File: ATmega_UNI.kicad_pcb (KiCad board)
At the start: 2 copper layers, 53.3 x 68.6 mm, 44 parts, among them J1 PDIP_1_to_14, J11 PDIP_1_to_14, J13 3.3V, J2 PDIP_15_to_28, J22 PDIP_15_to_28, J5 PWR_Jack, J611 I2C, J612 I2C, J62 4uni, J63 4uni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

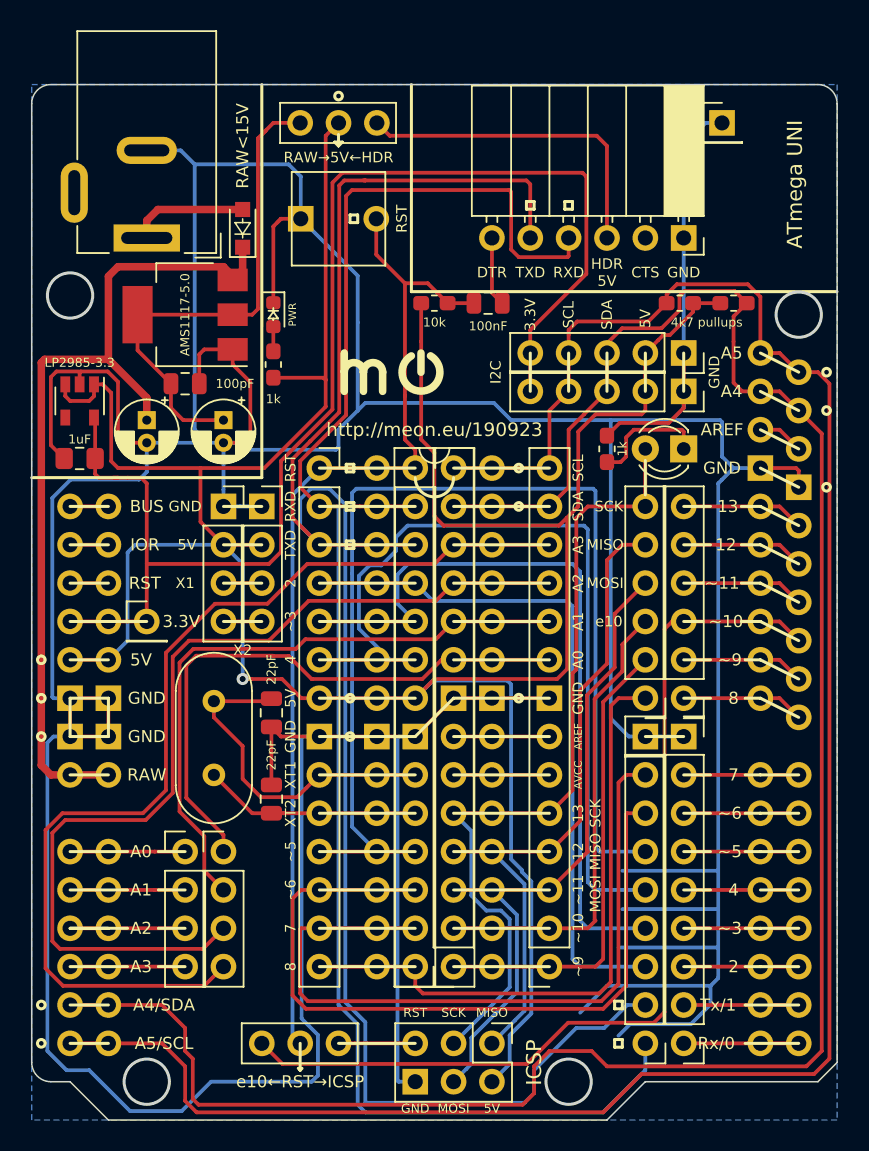
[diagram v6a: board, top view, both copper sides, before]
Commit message: move i2c to have more space for zif socket, wider 5V from raw tracks
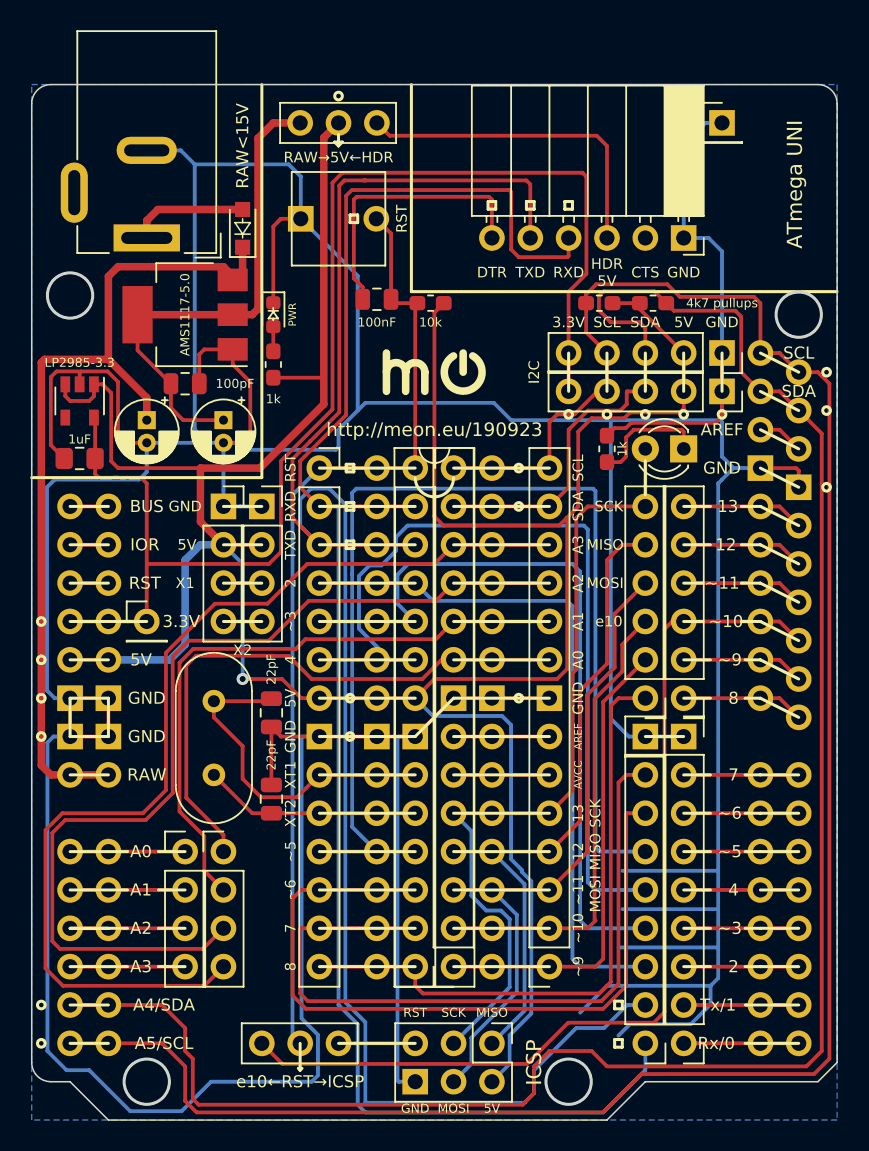
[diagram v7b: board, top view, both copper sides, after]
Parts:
- moved C2 7.37 mm to (88.9, 59.9), turned to 180 degrees
- moved R1 5.33 mm to (107.2, 60.2)
- moved R3 5.33 mm to (103.6, 60.2)
- moved REF** 2.79 mm to (92.7, 64.8)
- moved J611 2.54 mm to (111.8, 66.0)
- moved J612 2.54 mm to (111.8, 63.5)
- moved R2 0.25 mm to (92.5, 60.2), turned to 180 degrees
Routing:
- net DTR: track 4.60 -> 18.7 mm
- net GND: track 414.4 -> 423.5 mm
- net SDA: track 142.4 -> 148.1 mm
- net ~RST: track 68.0 -> 64.0 mm
- net SCL: track 139.5 -> 141.8 mm
- net +5V: track 196.3 -> 194.9 mm
- net +3V3: track 90.0 -> 89.0 mm
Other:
- net class wide added: clearance 0.2, trace_width 0.5, via_dia 0.8, via_drill 0.4

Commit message: move reset jumper a little further from icsp
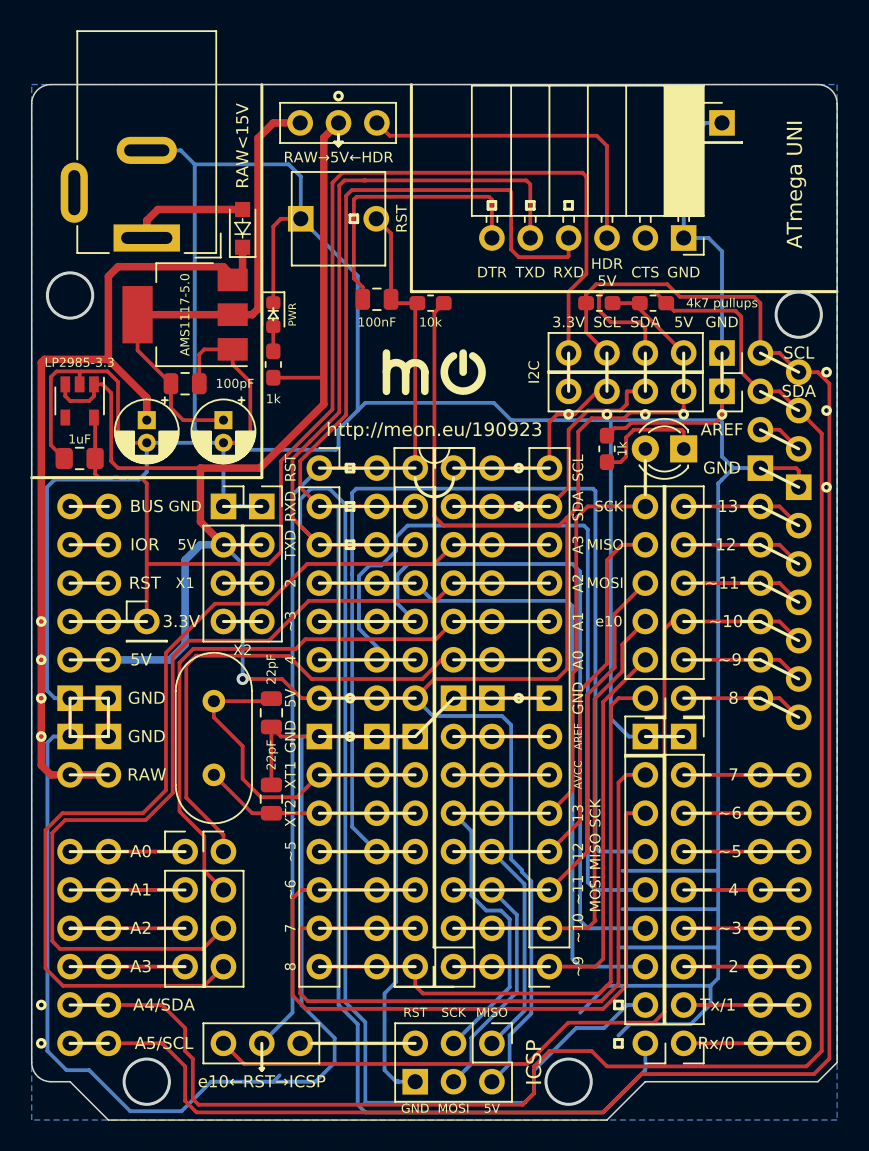
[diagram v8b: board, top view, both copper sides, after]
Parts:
- moved JP8 2.54 mm to (83.8, 109.2)
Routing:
- net ~iRST: track 5.08 -> 8.34 mm
- net GND: track 423.5 -> 426.1 mm
- net ~eRST: track 63.6 -> 66.2 mm
- net ~RST: track 64.0 -> 64.6 mm
